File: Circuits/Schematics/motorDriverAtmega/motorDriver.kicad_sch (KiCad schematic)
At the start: 19 parts, among them J1 Conn_01x04_Pin, J2 Conn_01x02_Pin, J3 Conn_01x03_Pin, J6 Conn_02x03_Counter_Clockwise, U1 MAX485E, U3 ATmega328P-A, Y2 Crystal_GND24

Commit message: Main PCB Sketches
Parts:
- removed J3: Conn_01x03_Pin, TerminalBlock_Phoenix:TerminalBlock_Phoenix_MKDS-1,5-3-5.08_1x03_P5.08mm_Horizontal, symbol Connector:Conn_01x03_Pin
- added J3: Screw_Terminal_01x03, TerminalBlock_Phoenix:TerminalBlock_Phoenix_PT-1,5-3-5.0-H_1x03_P5.00mm_Horizontal, symbol Connector:Screw_Terminal_01x03
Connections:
- net +5V: now also J3.3 (Pin_3)
- net GND: now also J3.2 (Pin_2)
- net VMOT: now also J3.1 (Pin_1)
- net RS-485 A: now reaches J2.1 (Pin_1), U1.6 (A)
- net RS-485 B: now reaches J2.2 (Pin_2), U1.7 (B)
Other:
- note added: "Bağlantılar"
- note added: "Polarize kapasitör (C4) mutlaka besleme geriliminin üstünde olacak. Besleme 24V ise tercihen 35V, 25V çok yakın kalır"
- note removed: "Polarize kapasitör mutlaka besleme geriliminin üstünde olacak. Besleme 24V ise tercihen 35V, 25V çok yakın kalır"
- note removed: "RS-485 A"
- note removed: "RS-485 B"

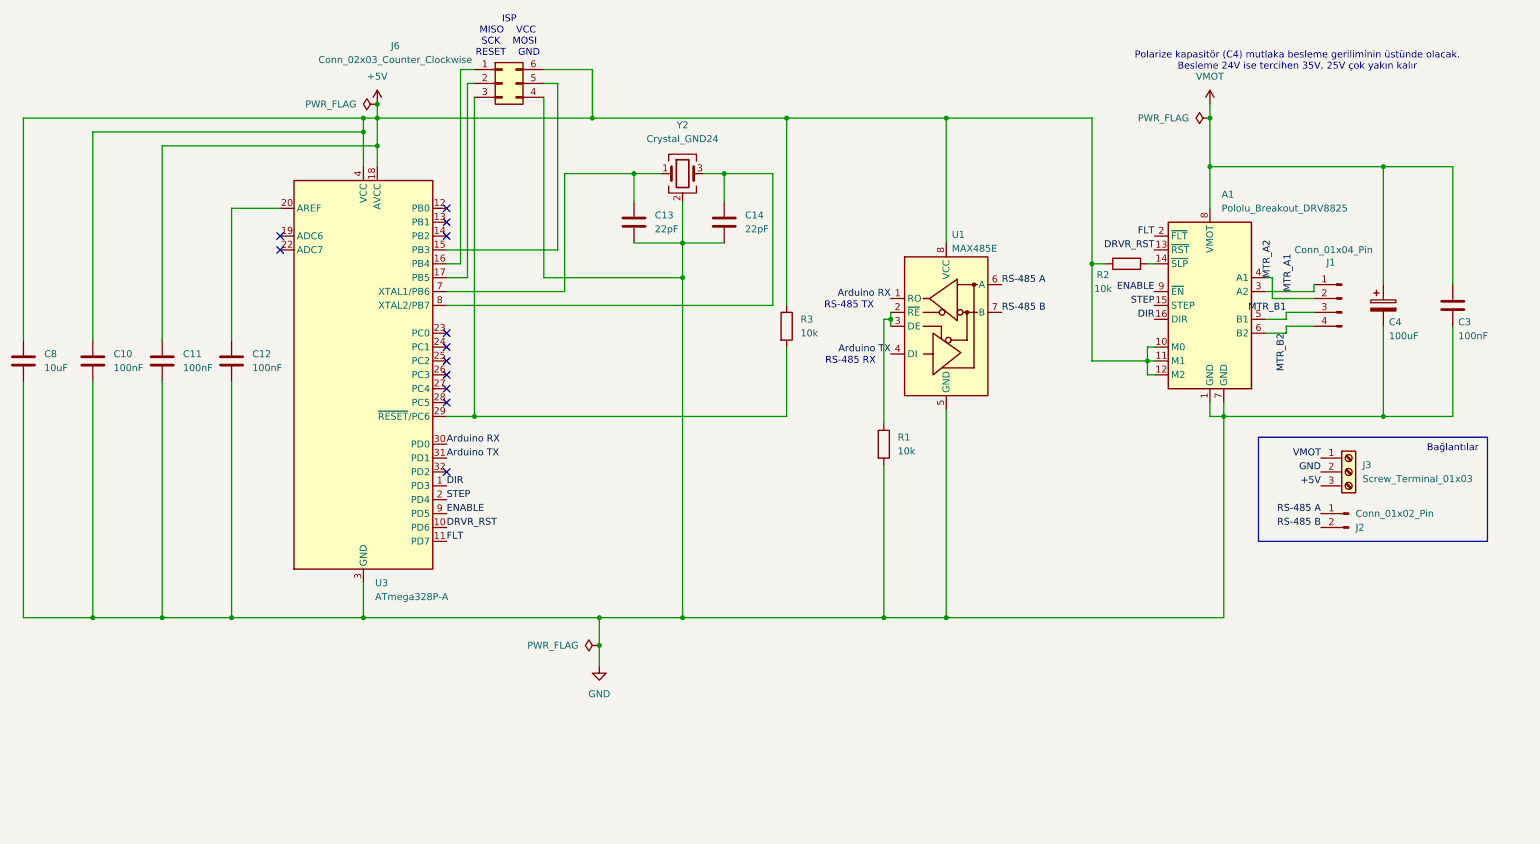
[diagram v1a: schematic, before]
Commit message: PCB Updates
Şematikler temize çekildi.
motorDriverAtmega hatalı RS-485 DE (pin 3) bağlantısı düzeltildi.
masterController şematiği tamamlandı.
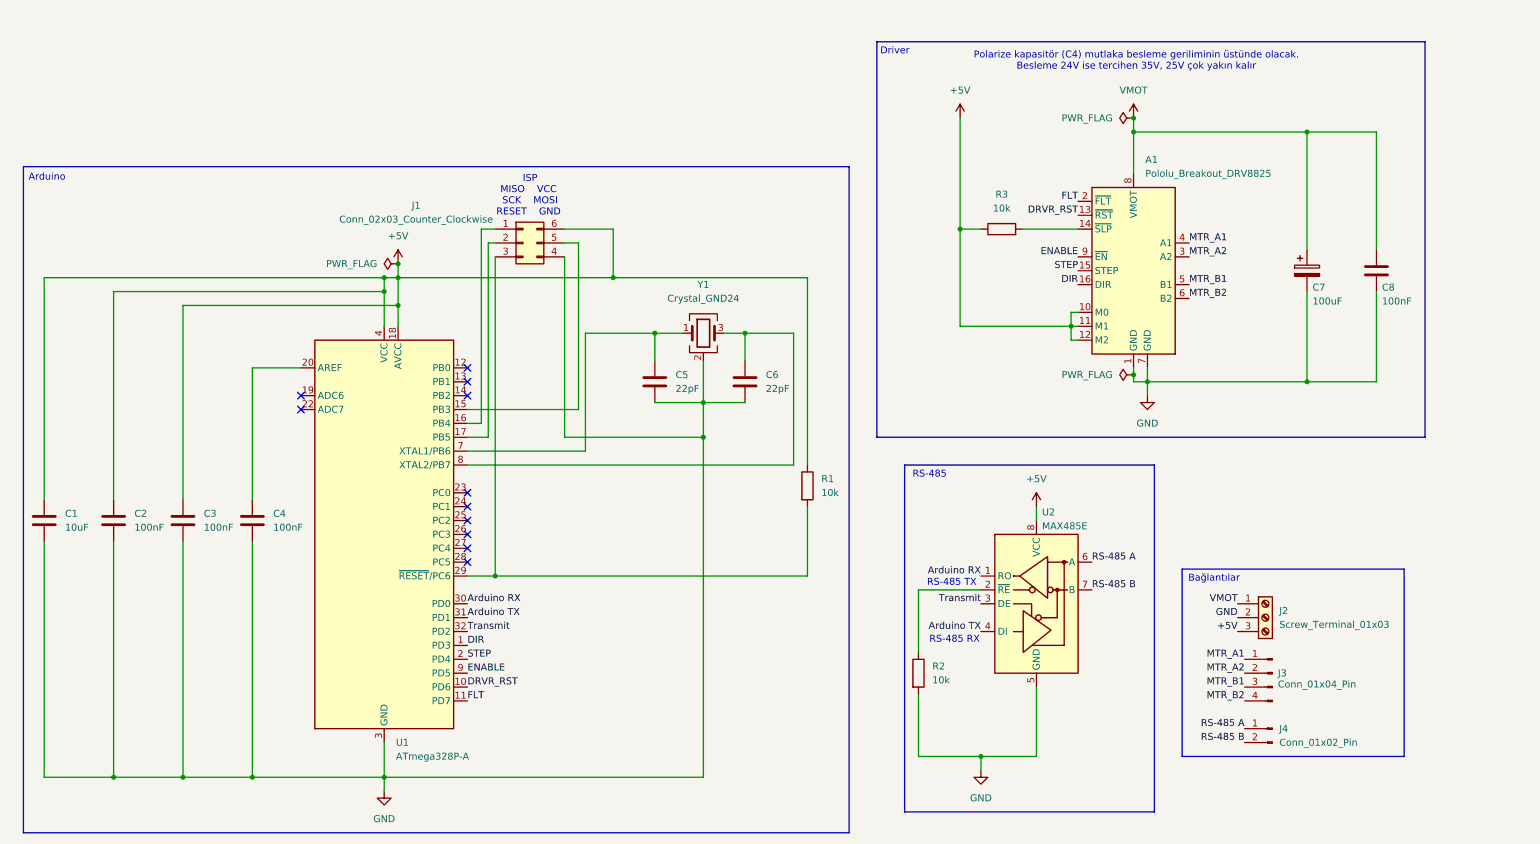
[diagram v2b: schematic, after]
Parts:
- removed J2: Conn_01x02_Pin, Connector_PinHeader_2.54mm:PinHeader_1x02_P2.54mm_Vertical, symbol Connector:Conn_01x02_Pin
- removed R2: 10k, Resistor_SMD:R_0805_2012Metric_Pad1.20x1.40mm_HandSolder, symbol Device:R
- added J4: Conn_01x02_Pin, symbol Connector:Conn_01x02_Pin
- added R3: 10k, symbol Device:R
- renumbered C8 to C1, C10 to C2, C11 to C3, C12 to C4, C13 to C5, C14 to C6, C4 to C7, C3 to C8, J6 to J1, J3 to J2, J1 to J3, R3 to R1, R1 to R2, U3 to U1, U1 to U2, Y2 to Y1
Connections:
- net +5V: now also R3.1
- net MTR_A1: now also A1.4 (A1); no longer A1.3 (A2)
- net MTR_A2: now also A1.3 (A2); no longer A1.4 (A1)
- net RS-485 A: now also J4.1 (Pin_1)
- net RS-485 B: now also J4.2 (Pin_2)
- net Transmit: now reaches U1.32 (PD2)
- net Transmit: now also U2.3 (DE)
- net at R2.1, U2.2 (~{RE}): no longer U2.3 (DE)
- net at A1.14 (~{SLP}): now also R3.2
- no-connect marks 12 -> 11
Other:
- note added: "Arduino"
- note added: "Driver"
- note added: "RS-485"
- moved on the sheet: A1, C1, C2, C3, C4, C5, C6, C7, C8, J1, J2, J3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

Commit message: Bug fixes, footprint assignments
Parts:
- C5, C6: value 22pF -> 18pF
- J4: footprint (none) -> Connector_PinHeader_2.54mm:PinHeader_1x02_P2.54mm_Vertical
- R3: footprint (none) -> Resistor_SMD:R_0805_2012Metric_Pad1.20x1.40mm_HandSolder
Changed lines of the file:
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@@
 	)
 	(junction
-		(at 83.82 58.42)
-		(diameter 0)
-		(color 0 0 0 0)
-	)
-	(junction
 		(at 81.28 63.5)
 		(diameter 0)
@@
 			)
 		)
-		(property "Value" "22pF"
+		(property "Value" "18pF"
 			(at 134.62 81.2799 0)
 			(show_name no)
@@
 	)
 	(symbol
-		(lib_id "power:PWR_FLAG")
-		(at 83.82 58.42 90)
-		(unit 1)
-		(body_style 1)
-		(exclude_from_sim no)
-		(in_bom yes)
-		(on_board yes)
-		(in_pos_files yes)
-		(dnp no)
-		(fields_autoplaced yes)
-		(property "Reference" "#FLG01"
-			(at 81.915 58.42 0)
-			(hide yes)
-			(show_name no)
-			(do_not_autoplace no)
-			(effects
-				(font
-					(size 1.27 1.27)
-				)
-			)
-		)
-		(property "Value" "PWR_FLAG"
-			(at 80.01 58.4199 90)
-			(show_name no)
-			(do_not_autoplace no)
-			(effects
-				(font
-					(size 1.27 1.27)
-				)
-				(justify left)
-			)
-		)
-		(property "Footprint" ""
-			(at 83.82 58.42 0)
-			(hide yes)
-			(show_name no)
-			(do_not_autoplace no)
-			(effects
-				(font
-					(size 1.27 1.27)
-				)
-			)
-		)
-		(property "Datasheet" ""
-			(at 83.82 58.42 0)
-			(hide yes)
-			(show_name no)
-			(do_not_autoplace no)
-			(effects
-				(font
-					(size 1.27 1.27)
-				)
-			)
-		)
-		(property "Description" "Special symbol for telling ERC where power comes from"
-			(at 83.82 58.42 0)
-			(hide yes)
-			(show_name no)
-			(do_not_autoplace no)
-			(effects
-				(font
-					(size 1.27 1.27)
-				)
-			)
-		)
-		(pin "1"
-		)
-		(instances
-			(project "motorDriver"
-				(path "/b811b567-d5fa-4982-b852-d277d0614258"
-					(reference "#FLG01")
-					(unit 1)
-				)
-			)
-		)
-	)
-	(symbol
 		(lib_id "Device:C")
 		(at 57.15 105.41 0)
@@
 			)
 		)
-		(property "Footprint" ""
+		(property "Footprint" "Connector_PinHeader_2.54mm:PinHeader_1x02_P2.54mm_Vertical"
 			(at 243.84 143.51 0)
 			(hide yes)
@@
 			)
 		)
-		(property "Footprint" ""
+		(property "Footprint" "Resistor_SMD:R_0805_2012Metric_Pad1.20x1.40mm_HandSolder"
 			(at 194.31 53.848 90)
 			(hide yes)
@@
 			)
 		)
-		(property "Value" "22pF"
+		(property "Value" "18pF"
 			(at 151.13 81.2799 0)
 			(show_name no)
@@
 					(unit 1)
 				)
+			)
+		)
+	)
+	(symbol
+		(lib_id "power:PWR_FLAG")
+		(at 237.49 125.73 180)
+		(unit 1)
+		(body_style 1)
+		(exclude_from_sim no)
+		(in_bom yes)
+		(on_board yes)
+		(in_pos_files yes)
+		(dnp no)
+		(fields_autoplaced yes)
+		(property "Reference" "#FLG01"
+			(at 237.49 127.635 0)
+			(hide yes)
+			(show_name no)
+			(do_not_autoplace no)
+			(effects
+				(font
+					(size 1.27 1.27)
+				)
+			)
+		)
+		(property "Value" "PWR_FLAG"
+			(at 237.49 130.81 0)
+			(hide yes)
+			(show_name no)
+			(do_not_autoplace no)
+			(effects
+				(font
+					(size 1.27 1.27)
+				)
+			)
+		)
+		(property "Footprint" ""
+			(at 237.49 125.73 0)
+			(hide yes)
+			(show_name no)
+			(do_not_autoplace no)
+			(effects
+				(font
+					(size 1.27 1.27)
+				)
+			)
+		)
+		(property "Datasheet" ""
+			(at 237.49 125.73 0)
+			(hide yes)
+			(show_name no)
+			(do_not_autoplace no)
+			(effects
+				(font
+					(size 1.27 1.27)
+				)
+			)
+		)
+		(property "Description" "Special symbol for telling ERC where power comes from"
+			(at 237.49 125.73 0)
+			(hide yes)
+			(show_name no)
+			(do_not_autoplace no)
+			(effects
+				(font
+					(size 1.27 1.27)
+				)
+			)
+		)
+		(pin "1"
+		)
+		(instances
+			(project "motorDriver"
+				(path "/b811b567-d5fa-4982-b852-d277d0614258"
+					(reference "#FLG01")
+					(unit 1)
+				)
